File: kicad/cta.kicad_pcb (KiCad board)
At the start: 2 copper layers, 49.5 x 49.5 mm, 25 parts, among them Q1 TIP120, Q2 KSP2907, U1 LM324

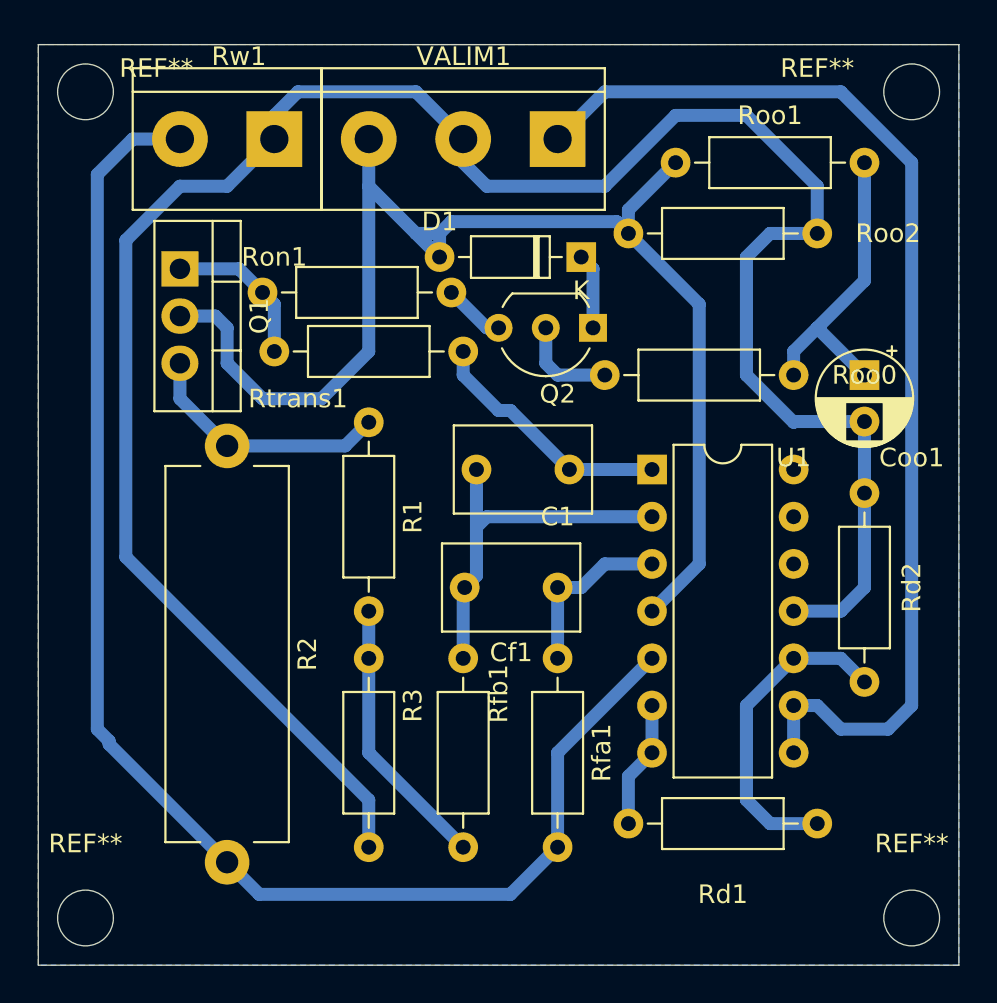
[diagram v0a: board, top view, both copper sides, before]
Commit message: Used the last op amp to implement an active low pass output filter
I think this is the best strategy to get a symmetric behavior when heating or cooling. Just get a time constant larger than the corresponding cooling time constant.
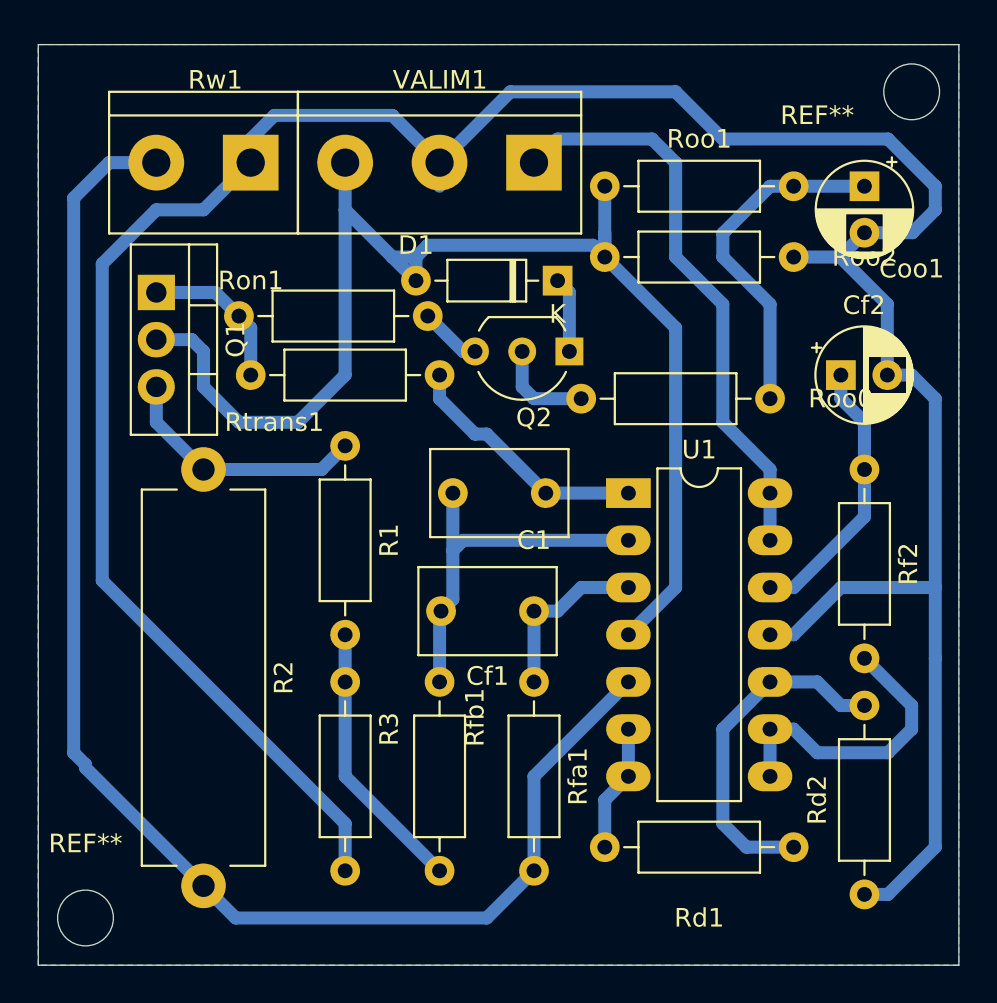
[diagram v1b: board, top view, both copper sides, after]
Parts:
- removed the REF** at (137.2, 110.5)
- removed the REF** at (92.7, 66.0)
- added Cf2: 10u, Capacitor_THT:CP_Radial_D5.0mm_P2.50mm, F.Cu at (133.3, 81.3)
- added Rf2: 10k, Resistor_THT:R_Axial_DIN0207_L6.3mm_D2.5mm_P10.16mm_Horizontal, F.Cu at (134.6, 86.4)
- U1: footprint Package_DIP:DIP-14_W7.62mm -> Package_DIP:DIP-14_W7.62mm_LongPads
- moved Rd2 21.6 mm to (134.6, 109.2), turned to 90 degrees
- moved Coo1 10.2 mm to (134.6, 71.1)
- moved Roo1 4.02 mm to (120.7, 71.1)
- moved C1 1.80 mm to (117.5, 87.6)
- moved Cf1 1.80 mm to (116.8, 94.0)
- moved Q1 1.80 mm to (96.5, 76.8)
- moved Q2 1.80 mm to (118.7, 80.0)
- moved R1 1.80 mm to (106.7, 85.1)
- moved R3 1.80 mm to (106.7, 97.8)
- moved Rd1 1.80 mm to (120.7, 106.7)
- moved Rfa1 1.80 mm to (116.8, 97.8)
- moved Rfb1 1.80 mm to (111.8, 97.8)
- moved Ron1 1.80 mm to (101.0, 78.1)
- moved Roo0 1.80 mm to (129.5, 82.5)
- moved Roo2 1.80 mm to (120.7, 74.9)
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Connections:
- U1 pad 12: (no net) -> Net-(Cf2-Pad1)
- U1 pad 13: (no net) -> /VOUTPUT
- U1 pad 14: (no net) -> /VOUTPUT
- U1 pad 8: /VOUTPUT -> Net-(Rf2-Pad2)
- U1 pad 9: /VOUTPUT -> Net-(Rf2-Pad2)
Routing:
- net GND: track 119.2 -> 152.3 mm
- net /VOUTPUT: track 60.8 -> 31.1 mm
- net Net-(Rf2-Pad2): track 0.00 -> 16.1 mm
- net Net-(Cf2-Pad1): track 0.00 -> 14.8 mm
- net Net-(Coo1-Pad1): track 16.6 -> 18.6 mm
- net Net-(Rd1-Pad2): track 17.3 -> 18.6 mm

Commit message: Added a decoupling capacitor to op amp and improved layout
I don't know if this will help but it may reduce noise and improve performance when voltage input is noisy.
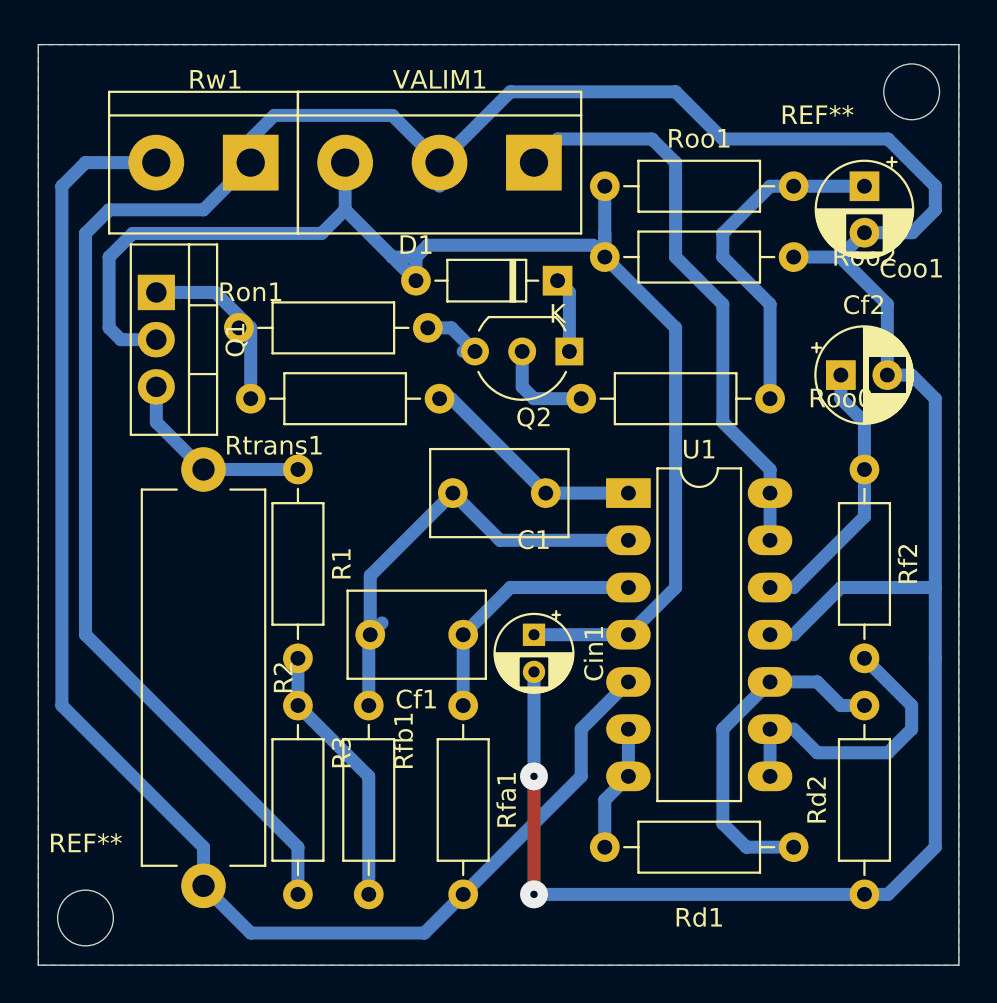
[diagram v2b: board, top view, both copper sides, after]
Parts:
- added Cin1: 100n, Capacitor_THT:CP_Radial_D4.0mm_P2.00mm, F.Cu at (116.8, 95.2)
- C1, Cf1: value 1u -> 10n
- Rfa1, Rfb1: value 47k -> 100
- moved Cf1 4.02 mm to (113.0, 95.2)
- moved Rfa1 4.02 mm to (113.0, 99.1)
- moved Rfb1 4.02 mm to (108.0, 99.1)
- moved R1 2.84 mm to (104.1, 86.4)
- moved R3 2.84 mm to (104.1, 99.1)
- moved Rtrans1 1.27 mm to (101.6, 82.5)
- moved Ron1 0.63 mm to (101.0, 78.7)
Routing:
- net GND: track 152.3 -> 184.5 mm, vias 0 -> 2
- net Net-(C1-Pad2): track 20.1 -> 24.7 mm
- net Net-(Cf1-Pad1): track 9.42 -> 13.8 mm
- net Net-(Q1-Pad3): track 13.6 -> 10.6 mm
- net VCC: track 72.2 -> 74.6 mm
- net Net-(Q1-Pad1): track 8.41 -> 9.68 mm
- net Net-(C1-Pad1): track 13.5 -> 12.3 mm
- net Net-(R1-Pad2): track 14.8 -> 14.3 mm
